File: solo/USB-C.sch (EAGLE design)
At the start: 27 parts

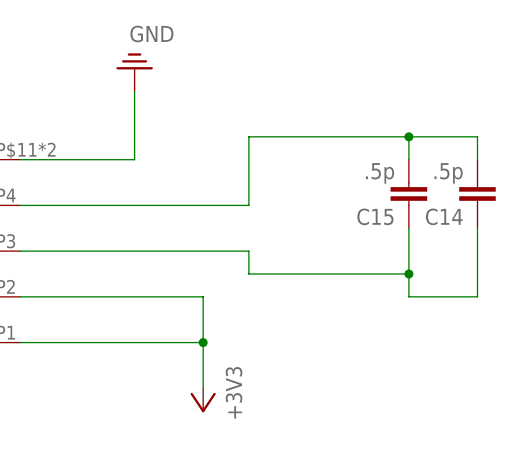
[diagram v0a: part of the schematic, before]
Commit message: update cap values
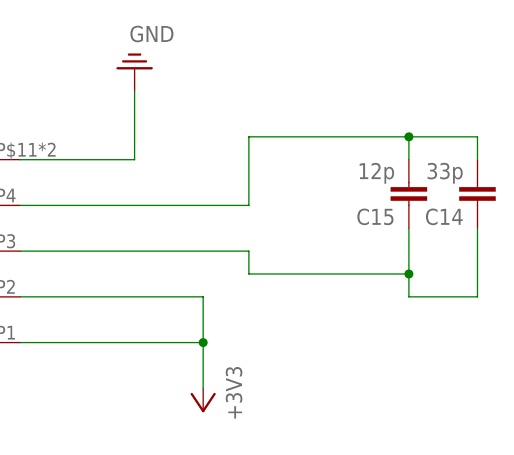
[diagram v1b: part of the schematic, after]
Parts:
- C14: value .5p -> 33p
- C15: value .5p -> 12p
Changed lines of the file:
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@@
 <part name="SUPPLY20" library="supply2" library_urn="urn:adsk.eagle:library:372" deviceset="PE" device="" value="GND"/>
 <part name="+3V8" library="supply1" library_urn="urn:adsk.eagle:library:371" deviceset="+3V3" device=""/>
-<part name="C15" library="efm-fido" library_urn="urn:adsk.eagle:library:4245354" deviceset="CAPACITOR" device="" package3d_urn="urn:adsk.eagle:package:4245806/9" value=".5p"/>
-<part name="C14" library="efm-fido" library_urn="urn:adsk.eagle:library:4245354" deviceset="CAPACITOR" device="" package3d_urn="urn:adsk.eagle:package:4245806/9" value=".5p"/>
+<part name="C15" library="efm-fido" library_urn="urn:adsk.eagle:library:4245354" deviceset="CAPACITOR" device="" package3d_urn="urn:adsk.eagle:package:4245806/9" value="12p"/>
+<part name="C14" library="efm-fido" library_urn="urn:adsk.eagle:library:4245354" deviceset="CAPACITOR" device="" package3d_urn="urn:adsk.eagle:package:4245806/9" value="33p"/>
 <part name="C3" library="efm-fido" library_urn="urn:adsk.eagle:library:4245354" deviceset="CAPACITOR" device="" package3d_urn="urn:adsk.eagle:package:4245806/9" value="4.7u"/>
 <part name="C7" library="efm-fido" library_urn="urn:adsk.eagle:library:4245354" deviceset="CAPACITOR" device="" package3d_urn="urn:adsk.eagle:package:4245806/9" value="4.7u"/>
